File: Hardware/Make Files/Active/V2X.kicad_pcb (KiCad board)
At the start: 2 copper layers, 272 parts, among them CON1 AVR-PDI-6, IC1 ATXMEGA16A4U-A, J1 DB9, P1 47553-1001, P10 Board Mount 2, P11 Ficudial2, P12 Board Mount 3, P13 Ficudial3, P14 5V0_OUT, P15 Board Mount 4, P16 Ficudial4, P17 CUR_SEN, P18 CUR_SEN, P19 CUR_SEN, P2 SMA, P20 Jumper 1, P21 Jumper 2, P22 CONN_02X04, P23 Jumper 3, P24 Jumper 4, P25 CONN_02X08, P26 CONN_02X08, P3 SMA, P5 NVM_RST, P6 Board Mount 1, P7 Ficudial1, P8 Open Source, P9 USB_u, Q1 2N7000, Q10 2N3904, Q11 IRF9335, Q12 IRF9335, Q13 BSS84, Q14 IRF9335, Q15 2N7000, Q16 2N7000, Q17 2N7000, Q18 2N7000, Q19 2N7000, Q2 BSS84, Q3 BSS84, Q4 BSS84, Q5 3906, Q6 2N3904, Q7 2N7000, Q8 2N3904, Q9 2N3904, SW1 SPST, SW2 SW_PUSH, U1 FT4232H, U10 MCP2551, U11 XRP6124, U12 SLG59M, U13 SLG59M, U14 XRP6124, U15 SLG59M, U16 SLG59M, U17 XRP6124, U18 SLG59M, U19 ADXL345, U2 93C46, U20 USB2242, U21 74LS126, U22 74HC595, U23 74HC595, U3 MMQA5V6T3G, U4 SIM5320, U5 ESDAxxSC6, U6 ESDAxxSC6, U7 STN1110, U8 LM339, U9 LM317, X1 12MHz, X2 16MHz, X3 24MHz

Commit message: Build pass of main V2X board
ready to verify
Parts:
- removed D3, D5: RED, LEDs:LED-0805
- removed D4, D6: BLUE, LEDs:LED-0805
- removed R16, R17, R18, R19: 330, Custom Parts:R_0603_sm
- removed R60: 0, Custom Parts:R_0603_sm
- removed U13: SLG59M, Custom Parts:STDFN-4
- added REF**: Rpi2B, Custom Parts:Rpi2B, F.Cu at (108.0, 125.0)
- C1, C10, C11, C12, C13, C2, C29, C3, C30, C31, C33, C36, C4, C44, C5, C51, C56, C57, C6, C60, C63, C64, C69, C8, C9, D1, D11, D15, D18, D2, F2, FB1, FB2, FB4, FB6, R1, R15, R20, R22, R24, R28, R30, R31, R35, R37, R38, R39, R4, R40, R41, R47, R48, R49, R5, R50, R51, R55, R57, R58, R6, R61, R7, R72, R75, R79, R81, R82, R83, R87, R88, R89, R92, R93, R94, R96, U11, U17, U8: moved to B.Cu
- C42, P1, P2, P3, U4: moved to F.Cu
- CON1: value AVR-PDI-6 -> AVR PDI
- D16, D17, D20: footprint LEDs:LED-0805 -> Custom Parts:LED-0805-SM
- F1: value 1.1A -> 2A
- IC1: value ATXMEGA16A4U-A -> XMEGA16A4U
- P14: value 5V0_OUT -> HOST 5V0
- P17: value CUR_SEN -> 5V0 CUR SEN
- P19: value CUR_SEN -> 3V3 CUR SEN
- P5: footprint Connect:PINHEAD1-2 -> Custom Parts:R_0603_sm; moved to B.Cu
- Q1, Q10, Q16, Q17, Q18, Q19, Q2, Q4, Q6, Q7, Q9: footprint Housings_SOT-23_SOT-143_TSOT-6:SOT-23 -> Custom Parts:SOT-23-123; moved to B.Cu
- Q13, Q15, Q3, Q5, Q8: footprint Housings_SOT-23_SOT-143_TSOT-6:SOT-23 -> Custom Parts:SOT-23-123
- R33: value 8.87K -> 8K87
- R62: value 10.5K -> 10K5; moved to B.Cu
- R70, R73: value 10.5K -> 10K5
- SW2: footprint Custom Parts:SW_SPST_FSMSM_SM -> Custom Parts:PTS645VK58-2-LFS
- moved FB3 366.4 mm to (-88.0, -55.6)
- moved C16 362.5 mm to (-88.0, -55.6)
- moved C28 361.5 mm to (-88.0, -55.6)
- moved C27 359.8 mm to (-88.0, -55.6)
- moved U3 358.6 mm to (-88.0, -55.6)
- moved C25 358.5 mm to (-88.0, -55.6)
- moved L2 356.6 mm to (-88.0, -55.6)
- moved L1 354.8 mm to (-88.0, -55.6)
- moved C23 353.1 mm to (-88.0, -55.6)
- moved R8 352.3 mm to (-88.0, -55.6)
- moved C18 351.1 mm to (-88.0, -55.6)
- moved C15 350.7 mm to (-88.0, -55.6)
- moved C26 350.0 mm to (-88.0, -55.6)
- moved R9 347.4 mm to (-88.0, -55.6)
- moved R12 347.2 mm to (-88.0, -55.6)
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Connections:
- C64 pad 1: 3V3_D -> 3V3_F
- FB6 pad 2: 3V3_D -> 3V3_F
- IC1 pad 39: 3V3_D -> 3V3_F
- P18 pad 1: 4V1_A -> 4V1_B
- P25 pad 10: SEQ_WAKE -> (no net)
- R41 pad 2: (no net) -> CAN_TXD
- R85 pad 2: SEQ_WAKE -> PC_WAKE
- U2 pad 8: 3V3_A -> 3V3_B
- U22 pad 7: 5V0_C_EN -> (no net)
- U4 pad 52: (no net) -> PC_WAKE
- U7 pad 22: Net-(D5-Pad1) -> (no net)
- U7 pad 23: Net-(D4-Pad1) -> (no net)
- U7 pad 24: Net-(D3-Pad1) -> (no net)
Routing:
- net GND: track 0.00 -> 689.4 mm, vias 0 -> 78
- net 12V0_B: track 0.00 -> 164.2 mm, vias 0 -> 6
- net 3V3_B: track 0.00 -> 130.6 mm, vias 0 -> 11
- net 3V3_A: track 0.00 -> 117.4 mm, vias 0 -> 14
- net 4V1_EN: track 0.00 -> 90.8 mm, vias 0 -> 1
- net CAN_5V_SW: track 0.00 -> 84.5 mm, vias 0 -> 1
- net ~HUB_RESET: track 0.00 -> 77.6 mm, vias 0 -> 2
- net SIM_VBUS: track 0.00 -> 76.2 mm, vias 0 -> 6
- net ~FTDI_RESET: track 0.00 -> 76.1 mm, vias 0 -> 6
- net HUB_SUSP: track 0.00 -> 75.5 mm, vias 0 -> 2
- net HOST_SC: track 0.00 -> 70.9 mm, vias 0 -> 1
- net HUB_STATUS: track 0.00 -> 70.5 mm, vias 0 -> 3
- net CAN_L: track 0.00 -> 70.3 mm, vias 0 -> 2
- net HUB_SCL: track 0.00 -> 60.3 mm, vias 0 -> 4
- net 5V0_B: track 0.00 -> 60.3 mm, vias 0 -> 1
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- added copper zone on F.Cu, net 12V0_B
- added copper zone on F.Cu, net 3V3_A
- added copper zone on B.Cu, net GND
- added copper zone on F.Cu, net GND
- added copper zone on F.Cu, net Net-(C44-Pad1)
- added copper zone on F.Cu, net Net-(C51-Pad1)
- added copper zone on F.Cu, net Net-(D12-Pad1)
- added copper zone on F.Cu, net Net-(D14-Pad1)
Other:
- board outline added: 85 x 56 mm
- net class PWR added: clearance 0.2, trace_width 0.5, via_dia 0.6, via_drill 0.4
- board text added: "GPS"
- board text added: "M2M"
- board text added: "PWR"

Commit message: V1.2 pass complete and ready to order
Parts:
- removed C14, C25: 100N, Custom Parts:C_0603_SM
- removed C15, C17, C19, C47: 330P, Custom Parts:C_0603_SM
- removed C16: 0.1F, Capacitors_ThroughHole:C_Radial_D12.5_L25_P5
- removed C18, C20, C27: 10N, Custom Parts:C_0603_SM
- removed C21, C22: 47p, Custom Parts:C_0603_SM
- removed C23, C26: 220U, Capacitors_SMD:c_elec_6.3x5.8
- removed C24, C28, C46: 4U7, Custom Parts:C_0805_SM
- removed C48, C49: 10U, Custom Parts:C_1206_SM
- removed D13: SBR3U30P1-7, Diodes_SMD:SOD-123
- removed FB3: 220, Custom Parts:R_0603_sm
- removed L1, L2, L6, L7: 47N, Custom Parts:C_0603_SM
- removed L4: 5U6, Custom Parts:4.5x4.5mm_Ind
- removed P1: 47553-1001, Custom Parts:47553-1001
- removed P10: Board Mount 2, Mounting_Holes:MountingHole_3mm
- removed P12: Board Mount 3, Mounting_Holes:MountingHole_3mm
- removed P15: Board Mount 4, Mounting_Holes:MountingHole_3mm
- removed P18: CUR_SEN, Connect:PINHEAD1-2
- removed P2, P3: SMA, Custom Parts:SMA-RA_142-0701-801
- removed P26: CONN_02X08, Pin_Headers:Pin_Header_Straight_2x10
- removed P6: Board Mount 1, Mounting_Holes:MountingHole_3mm
- removed P8: Open Source, Symbols:Symbol_OSHW-Logo_CopperTop_BIG
- removed Q12: IRF9335, Custom Parts:SOIC-8_MOS
- removed R12, R13, R14: 22, Custom Parts:R_0603_sm
- removed R63: 2K0, Custom Parts:R_0603_sm
- removed R64: 8K2, Custom Parts:R_0603_sm
- removed R8, R84, R86, R9: DNS, Custom Parts:R_0603_sm
- removed R85: 0, Custom Parts:R_0603_sm
- removed U14: XRP6124, Housings_SOT-23_SOT-143_TSOT-6:SOT-23-5
- removed U3: MMQA5V6T3G, Housings_SOT-23_SOT-143_TSOT-6:SOT-23-6
- removed U4: SIM5320, Custom Parts:SIM5320
- P11, P20, P23, P24: moved to B.Cu
- Q1, Q10, Q13, Q15, Q16, Q17, Q18, Q19, Q2, Q3, Q4, Q5, Q6, Q7, Q8, Q9: footprint Custom Parts:SOT-23-123 -> Custom Parts:SOT_23_123
- moved P23 166.8 mm to (112.0, 74.0)
- moved P7 165.8 mm to (112.0, 74.0)
- moved P24 150.8 mm to (112.0, 127.0)
- moved P16 131.5 mm to (112.0, 127.0)
- moved P11 118.9 mm to (184.0, 74.0)
- moved P13 105.1 mm to (184.0, 74.0)
- moved P20 85.4 mm to (184.0, 127.0)
- moved P21 55.3 mm to (184.0, 127.0)
- moved C56 4.43 mm to (181.0, 80.0), turned to 90 degrees
- moved Q10 1.00 mm to (170.0, 102.0)
- moved Q9 0.50 mm to (170.0, 106.5)
- moved R57 0.50 mm to (164.0, 102.5)
- moved R58 0.50 mm to (166.5, 102.5)
- moved D16 0.20 mm to (106.7, 108.0)
- moved D17 0.20 mm to (106.7, 97.0)
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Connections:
- J1 pad : (no net) -> GND
- REF** pad : (no net) -> GND
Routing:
- net 12V0_B: track 164.2 -> 63.1 mm
- net GND: track 689.4 -> 771.6 mm, vias 78 -> 101
- net Net-(Q5-Pad1): track 11.5 -> 2.52 mm, vias 1 -> 0
- net Net-(C44-Pad1): track 13.5 -> 4.86 mm
- net HOST_SC: track 70.9 -> 62.7 mm
- net Net-(C56-Pad1): track 7.50 -> 15.4 mm
- net K-LINE: track 24.8 -> 17.1 mm
- net SR_LATCH: track 35.4 -> 30.9 mm
- net SIM_PWR_ON: track 39.3 -> 43.2 mm
- net 3V3_A: track 117.4 -> 113.9 mm, vias 14 -> 13
- net SIMCARD: track 47.5 -> 45.3 mm, vias 4 -> 2
- net 4V1_EN: track 90.8 -> 88.9 mm
- net SIM_VBUS: track 76.2 -> 74.5 mm
- net HUB_SUSP: track 75.5 -> 73.9 mm
- net ~FTDI_RESET: track 76.1 -> 74.6 mm
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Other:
- board text added: "JAGUR LAND ROVER OSTC RVI V2X V1.2 2015"
- board text added: "Jesse Banks"
- board text added: "PWR+SEQ+OBD+ACL BOARD"

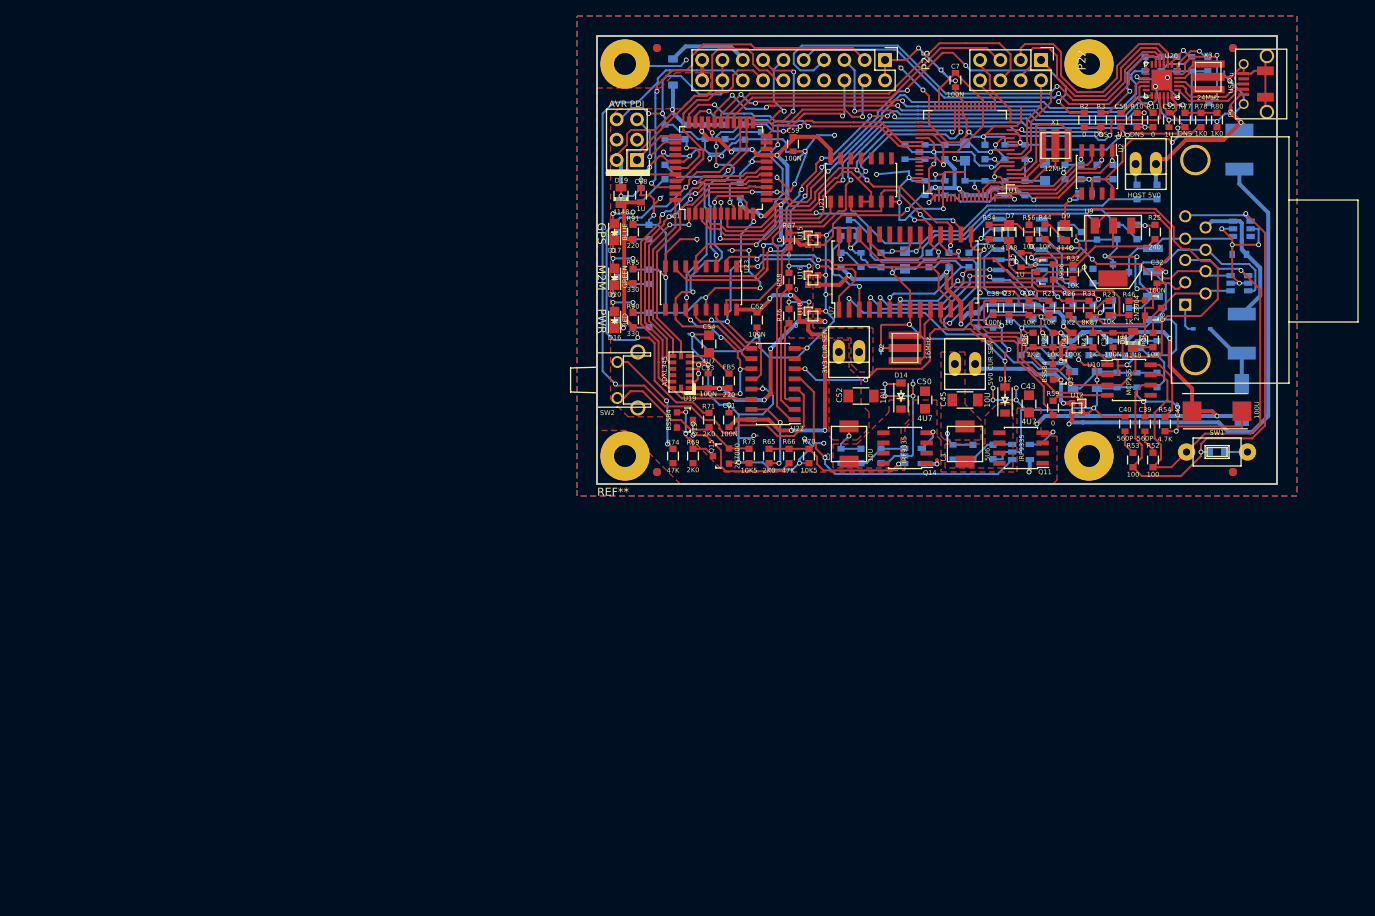
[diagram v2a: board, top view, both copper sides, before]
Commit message: Project rework
Split the Main and GSM boards into separate projects, redesigned Main
board after flaws were found.
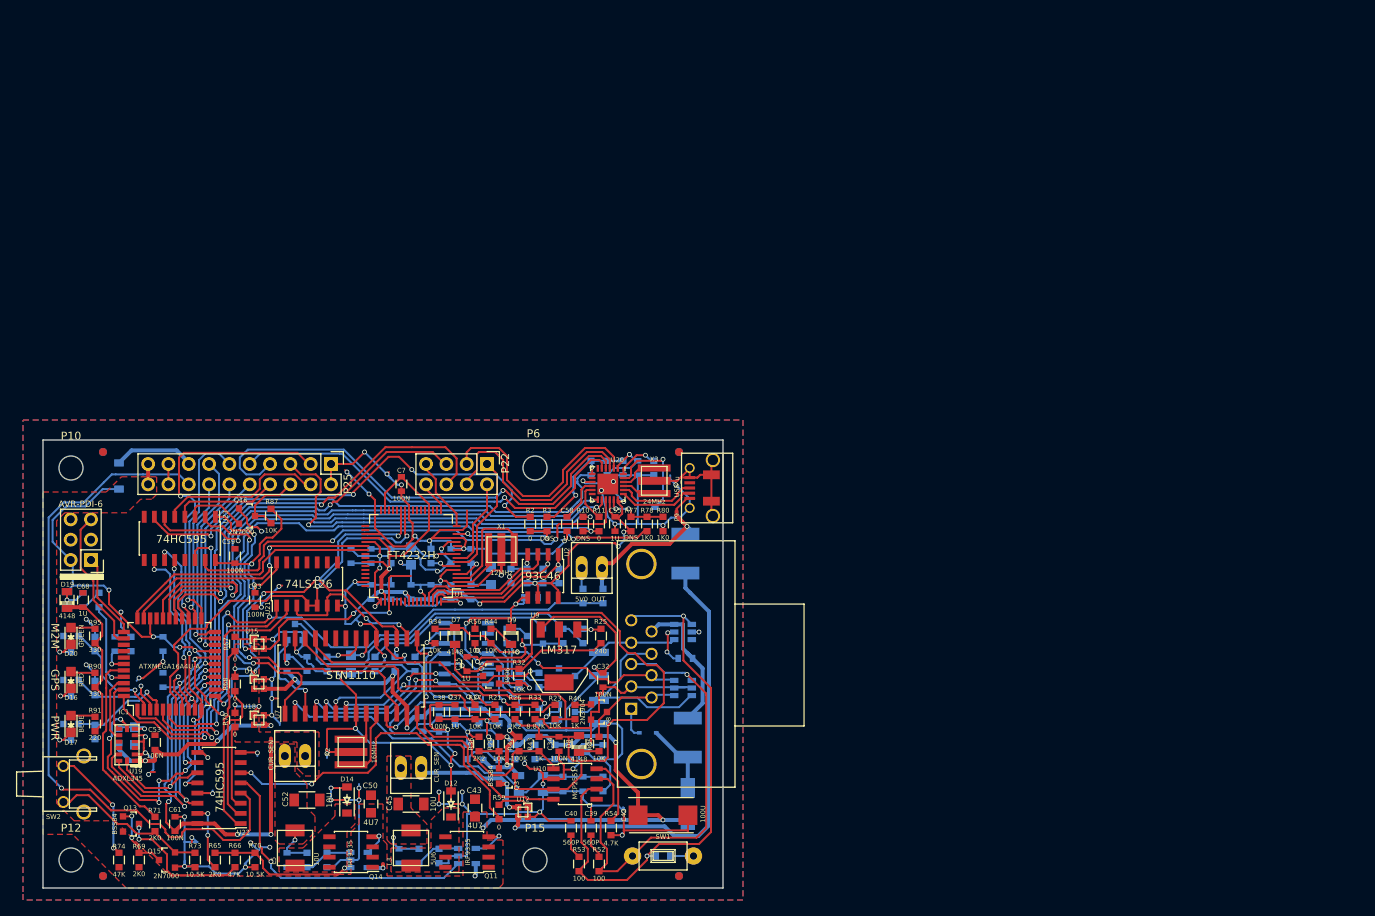
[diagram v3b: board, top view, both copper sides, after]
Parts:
- removed REF**: Rpi2B, Custom Parts:Rpi2B
- added P10: Board Mount 2, Mounting_Holes:MountingHole_3mm, F.Cu at (38.8, 126.5)
- added P12: Board Mount 3, Mounting_Holes:MountingHole_3mm, F.Cu at (38.8, 175.5)
- added P15: Board Mount 4, Mounting_Holes:MountingHole_3mm, F.Cu at (96.8, 175.5)
- added P6: Board Mount 1, Mounting_Holes:MountingHole_3mm, F.Cu at (96.8, 126.5)
- C54, C62, FB5: moved to B.Cu
- C63, Q16, R87: moved to F.Cu
- CON1: value AVR PDI -> AVR-PDI-6
- F1: value 2A -> 1.1A
- IC1: value XMEGA16A4U -> ATXMEGA16A4U-A
- P14: value HOST 5V0 -> 5V0_OUT
- P17: value 5V0 CUR SEN -> CUR_SEN
- P19: value 3V3 CUR SEN -> CUR_SEN
- R33: value 8K87 -> 8.87K
- R62, R70, R73: value 10K5 -> 10.5K
- moved FB6 94.3 mm to (46.2, 148.5)
- moved C64 93.9 mm to (44.2, 148.5)
- moved Q18 93.3 mm to (38.8, 159.5), turned to 0 degrees
- moved R93 93.3 mm to (41.8, 159.5), turned to 90 degrees
- moved C60 93.2 mm to (50.2, 148.5)
- moved IC1 92.7 mm to (51.0, 151.0)
- moved D17 91.6 mm to (38.8, 158.5)
- moved R91 91.1 mm to (41.8, 158.5)
- moved R94 88.7 mm to (42.2, 143.0), turned to 270 degrees
- moved FB5 88.2 mm to (44.8, 160.0)
- moved C54 86.9 mm to (46.8, 160.0), turned to 270 degrees
- moved C62 86.8 mm to (50.2, 153.0), turned to 90 degrees
- moved C59 86.7 mm to (59.2, 137.5), turned to 90 degrees
- moved C68 86.2 mm to (40.2, 143.0)
- moved C69 86.2 mm to (40.2, 143.0)
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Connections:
- IC1 pad 1: ACL_INT2 -> HUB_SUSP
- IC1 pad 13: (no net) -> CAN_RXD_PS_BUF
- IC1 pad 2: HUB_STATUS -> SEQ_LED1
- IC1 pad 20: (no net) -> SEQ_WAKE
- IC1 pad 21: (no net) -> SIM_NET
- IC1 pad 24: SEQ-CHGPUMP -> SIM_PWR
- IC1 pad 25: BUTTON -> SIMCARD
- IC1 pad 3: HUB_SUSP -> SEQ_LED2
- IC1 pad 4: HOST_SC -> SEQ_LED3
- IC1 pad 40: SIM_NET -> BUTTON
- IC1 pad 41: SIM_PWR -> SEQ-CHGPUMP
- IC1 pad 42: SIMCARD -> ACL_INT2
- IC1 pad 43: (no net) -> ACL_INT1
- IC1 pad 44: ACL_INT1 -> HUB_STATUS
- IC1 pad 5: (no net) -> HOST_SC
- P25 pad 10: (no net) -> SEQ_WAKE
- P25 pad 6: SIM_PWR_ON -> ~SIM_PWR_ON
- P25 pad 8: (no net) -> ~SIM_RESET
- Q17 pad 2: PC_LED1 -> SEQ_LED2
- Q18 pad 2: PC_LED2 -> SEQ_LED3
- Q19 pad 2: PC_LED3 -> SEQ_LED1
- R92 pad 2: PC_LED1 -> SEQ_LED2
- R93 pad 2: PC_LED2 -> SEQ_LED3
- R96 pad 2: PC_LED3 -> SEQ_LED1
- SW2 pad S: (no net) -> GND
- U21 pad 2: (no net) -> CAN_RXD_PS_BUF
- U23 pad 1: ~CAN_RESET -> ~CAN_SLEEP
- U23 pad 2: ~CAN_SLEEP -> ~CAN_RESET
- U23 pad 4: (no net) -> ~SIM_RESET
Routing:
- net GND: track 771.6 -> 579.0 mm, vias 101 -> 81
- net SIM_PWR_ON: track 43.2 -> 7.65 mm, vias 5 -> 0
- net BUTTON: track 57.4 -> 23.4 mm, vias 2 -> 0
- net Net-(U22-Pad9): track 7.05 -> 32.1 mm, vias 0 -> 2
- net SEQ_WAKE: track 0.00 -> 25.0 mm, vias 0 -> 1
- net 3V3_A: track 113.9 -> 138.8 mm, vias 13 -> 12
- net HUB_STATUS: track 70.1 -> 93.7 mm, vias 3 -> 1
- net SIM_RF_OFF: track 43.2 -> 21.3 mm, vias 3 -> 0
- net SEQ_MOSI: track 50.1 -> 31.1 mm
- net HUB_SUSP: track 73.9 -> 92.6 mm
- net CAN_RXD_PS_BUF: track 0.00 -> 17.8 mm
- net ~HUB_RESET: track 77.5 -> 60.2 mm
- net ~CAN_RESET: track 21.4 -> 37.7 mm
- net ~FTDI_RESET: track 74.6 -> 58.5 mm, vias 6 -> 4
- net SIM_VBUS: track 74.5 -> 58.7 mm, vias 6 -> 2
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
